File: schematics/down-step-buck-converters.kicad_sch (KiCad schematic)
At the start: 12 parts, among them U1 TPS54308

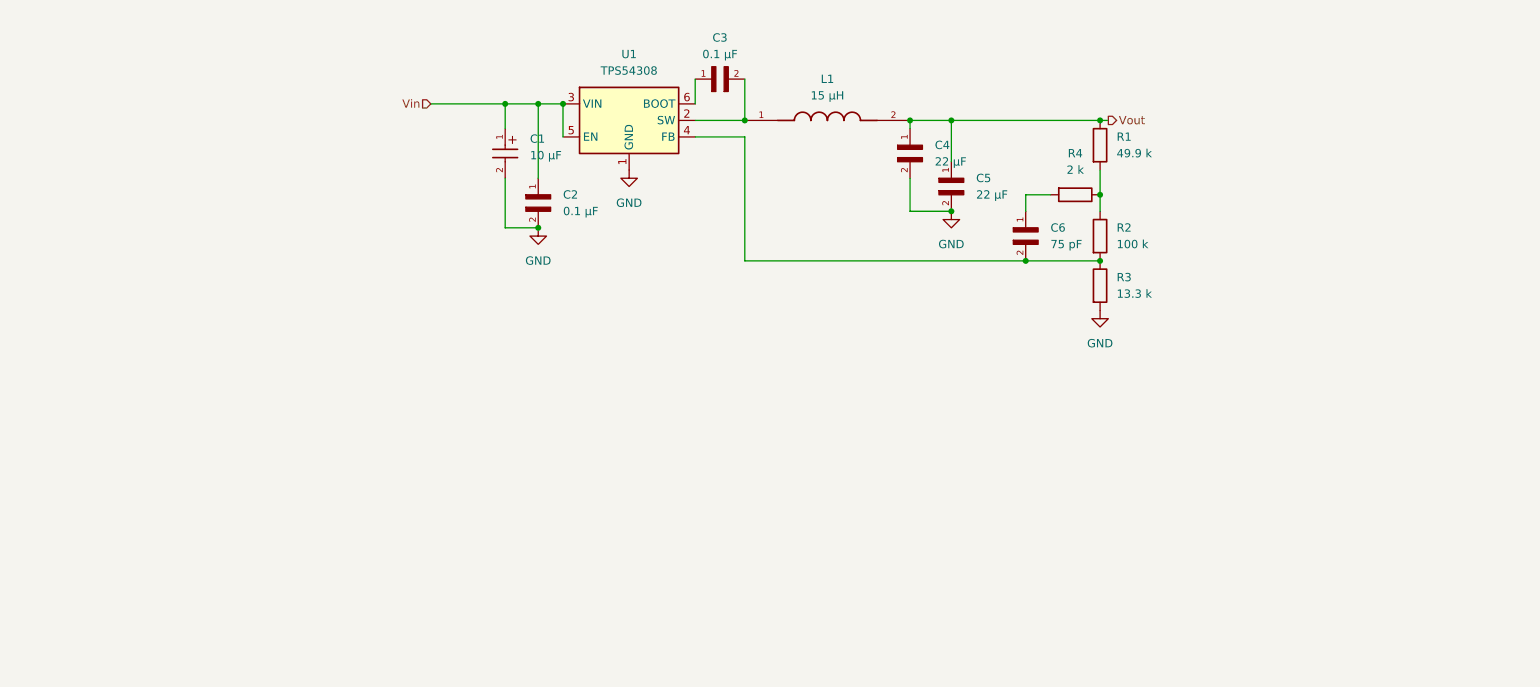
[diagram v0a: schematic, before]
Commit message: Integrated 3V3 buck converter due to Arduino's current limits
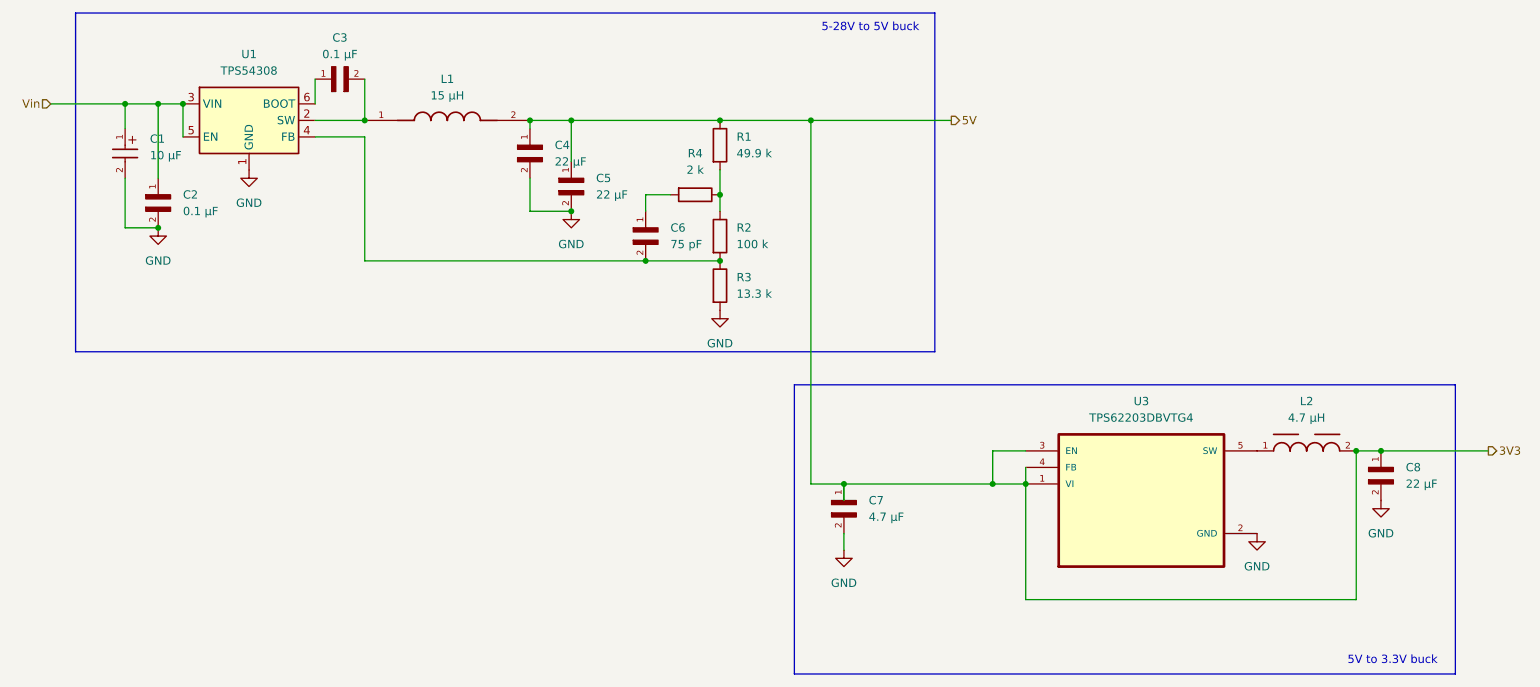
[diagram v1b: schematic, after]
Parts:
- added C7: 4.7 µF, MCASL21GBC7475MTCA01:CAPC2012X145N, symbol MCASL21GBC7475MTCA01:MCASL21GBC7475MTCA01
- added C8: 22 µF, MLASG32MSB5226MPNA01:CAPC3225X270N, symbol MLASG32MSB5226MPNA01:MLASG32MSB5226MPNA01
- added L2: 4.7 µH, WE-TPC_2828:WE-TPC_2828, symbol WE-TPC_2828:WE-TPC_2828
- added U3: TPS62203DBVTG4, TPS62203DBVTG4:SOT95P280X145-5N, symbol TPS62203DBVTG4:TPS62203DBVTG4
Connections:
- net GND: now also C7.2, C8.2, U3.2 (GND)
- net Vout renamed 3V3
- net 3V3: now also C7.1, C8.1, L2.2, U3.1 (VI), U3.3 (EN), U3.4 (FB)
- new net: L2.1, U3.5 (SW)
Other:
- note added: "5-28V to 5V buck"
- note added: "5V to 3.3V buck"
- title: 12V CC / 5V CC buck via TPS54308 -> 12V to 5V + 3.3V buck
- moved on the sheet: C1, C2, C3, C4, C5, C6, L1, R1, R2, R3, R4, U1
